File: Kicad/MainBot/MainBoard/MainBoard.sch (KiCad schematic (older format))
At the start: 37 parts, among them J1 Conn_01x02, J10 Conn_01x24, J11 01x24, J12 Conn_01x05, J13 Conn_01x03, J14 Conn_01x03, J15 Conn_01x03, J16 Conn_01x04, J17 Conn_01x04, J18 Conn_01x04, J19 Conn_01x04, J20 Conn_01x03, U1 AZ1117-3.3, U2 TCA9548A, U3 Teensy3.6, U4 DRV8825, U5 DRV8825, U6 DRV8825, U7 DRV8825

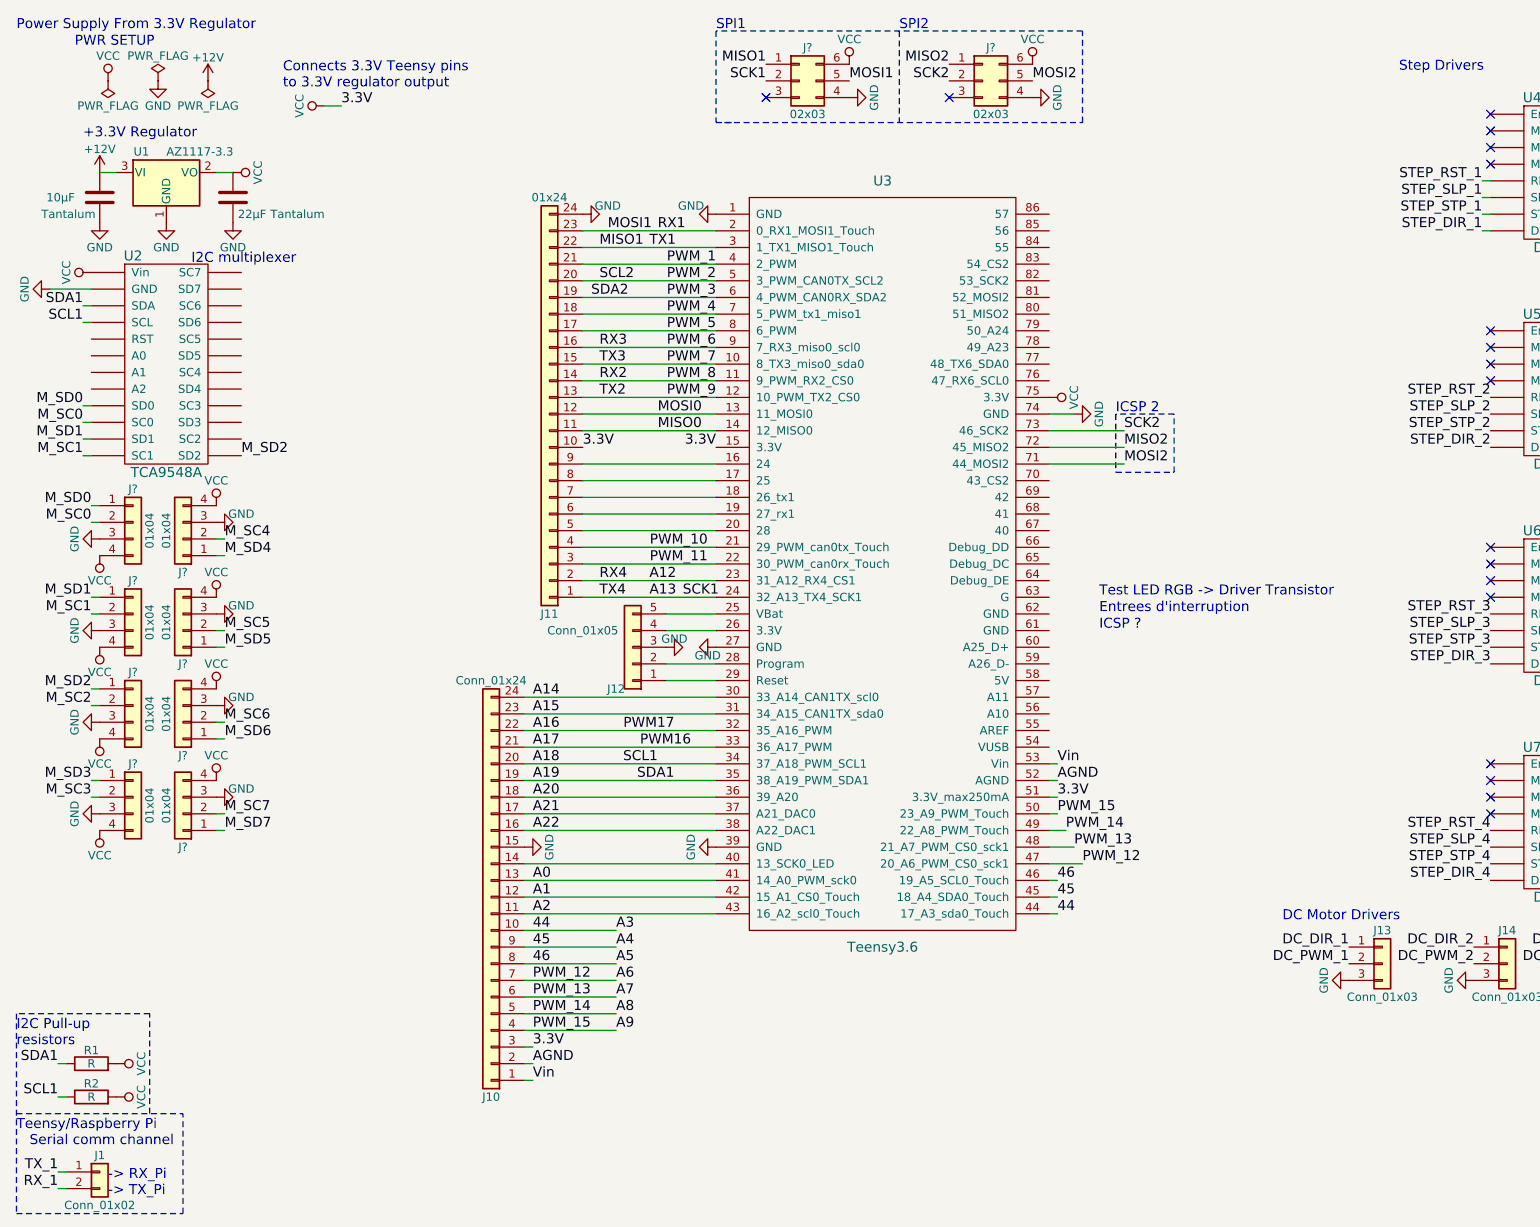
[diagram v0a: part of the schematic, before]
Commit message: Finished Multiplexer output, added pulled up resistors to multiplexer output
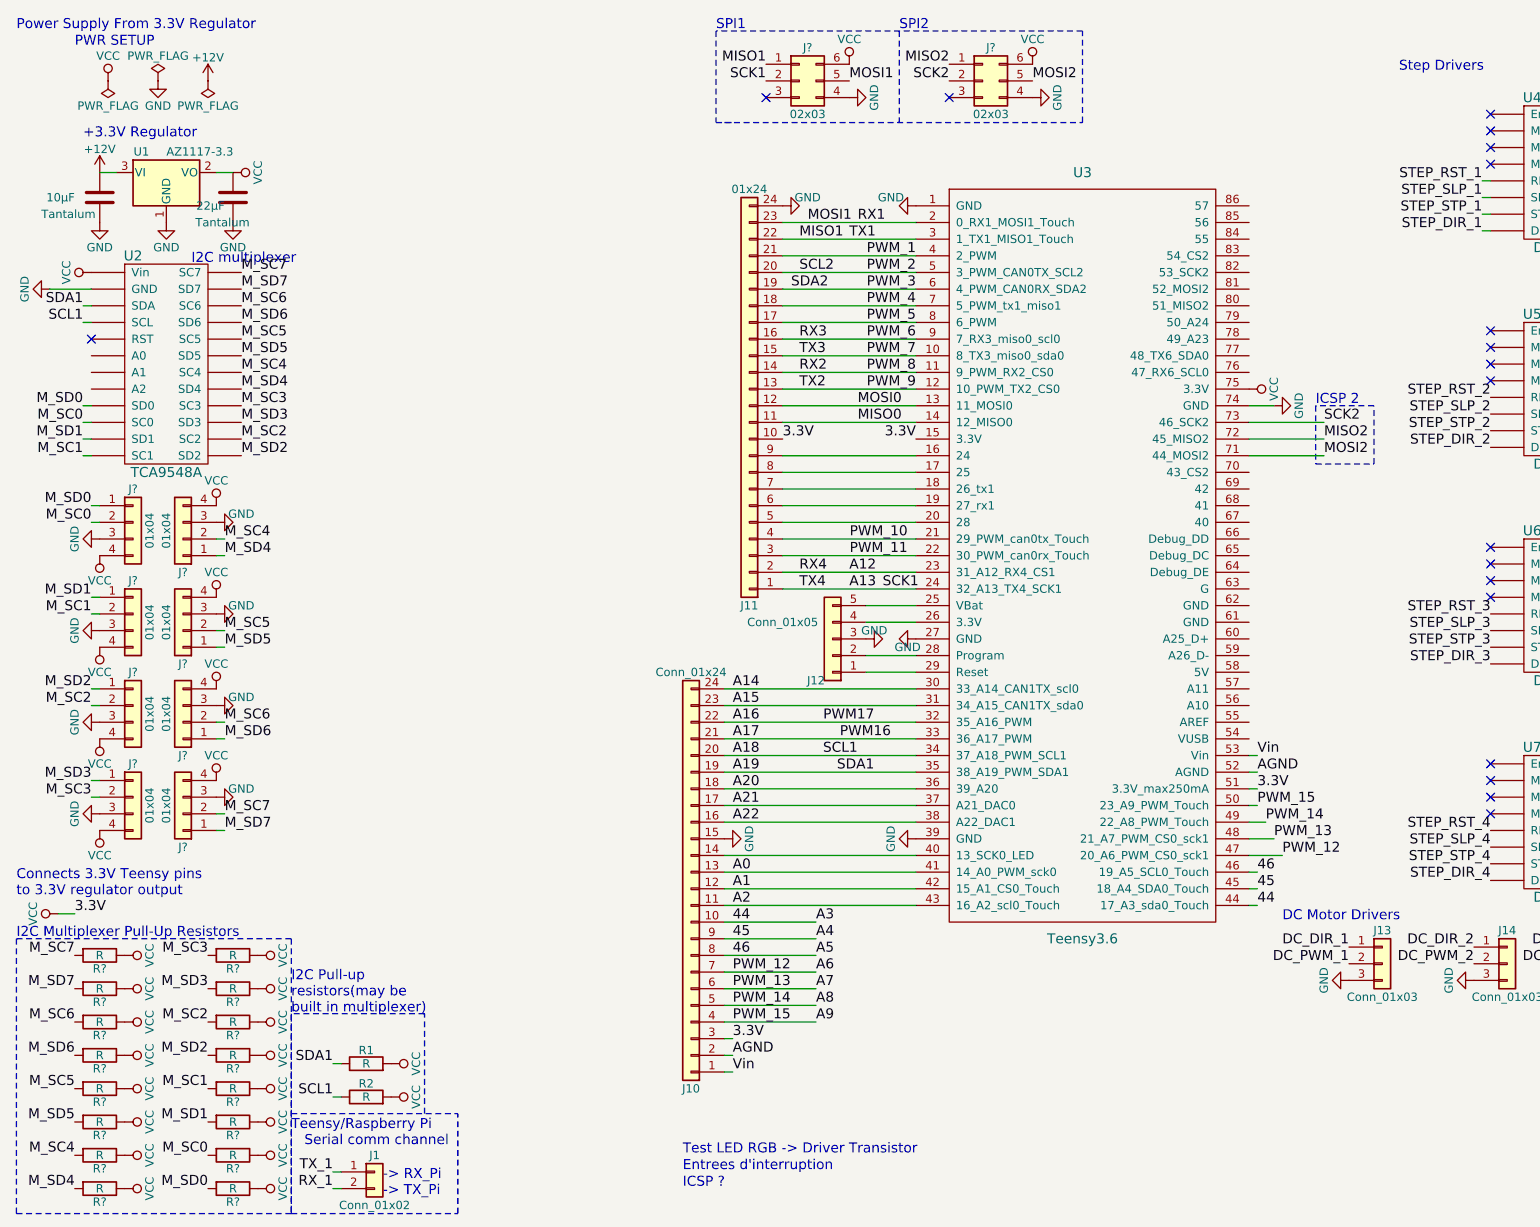
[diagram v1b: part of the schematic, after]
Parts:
- added R? (x16): R, symbol R
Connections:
- net M_SC0: now also R?.2
- net M_SC1: now also R?.2
- net M_SC2: now also U2.~ (Vin), R?.2
- net M_SC3: now also U2.~ (Vin), R?.2
- net M_SC4: now also U2.~ (Vin), R?.2
- net M_SC5: now also U2.~ (Vin), R?.2
- net M_SC6: now also U2.~ (Vin), R?.2
- net M_SC7: now also U2.~ (Vin), R?.2
- net M_SD0: now also R?.2
- net M_SD1: now also R?.2
- net M_SD2: now also R?.2
- net M_SD3: now also U2.~ (Vin), R?.2
- net M_SD4: now also U2.~ (Vin), R?.2
- net M_SD5: now also U2.~ (Vin), R?.2
- net M_SD6: now also U2.~ (Vin), R?.2
- net M_SD7: now also U2.~ (Vin), R?.2
- net VCC: now also R?.1, R?.1, R?.1, R?.1, R?.1, R?.1, R?.1, R?.1, R?.1, R?.1, R?.1, R?.1, R?.1, R?.1, R?.1, R?.1
- no-connect marks 22 -> 23
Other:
- note added: "I2C Multiplexer Pull-Up Resistors\n"
- note added: "I2C Pull-up\nresistors(may be \nbuilt in multiplexer)\n\n"
- note removed: "I2C Pull-up\nresistors\n"
- moved on the sheet: J1, J10, J11, J12, R1, R2, U3

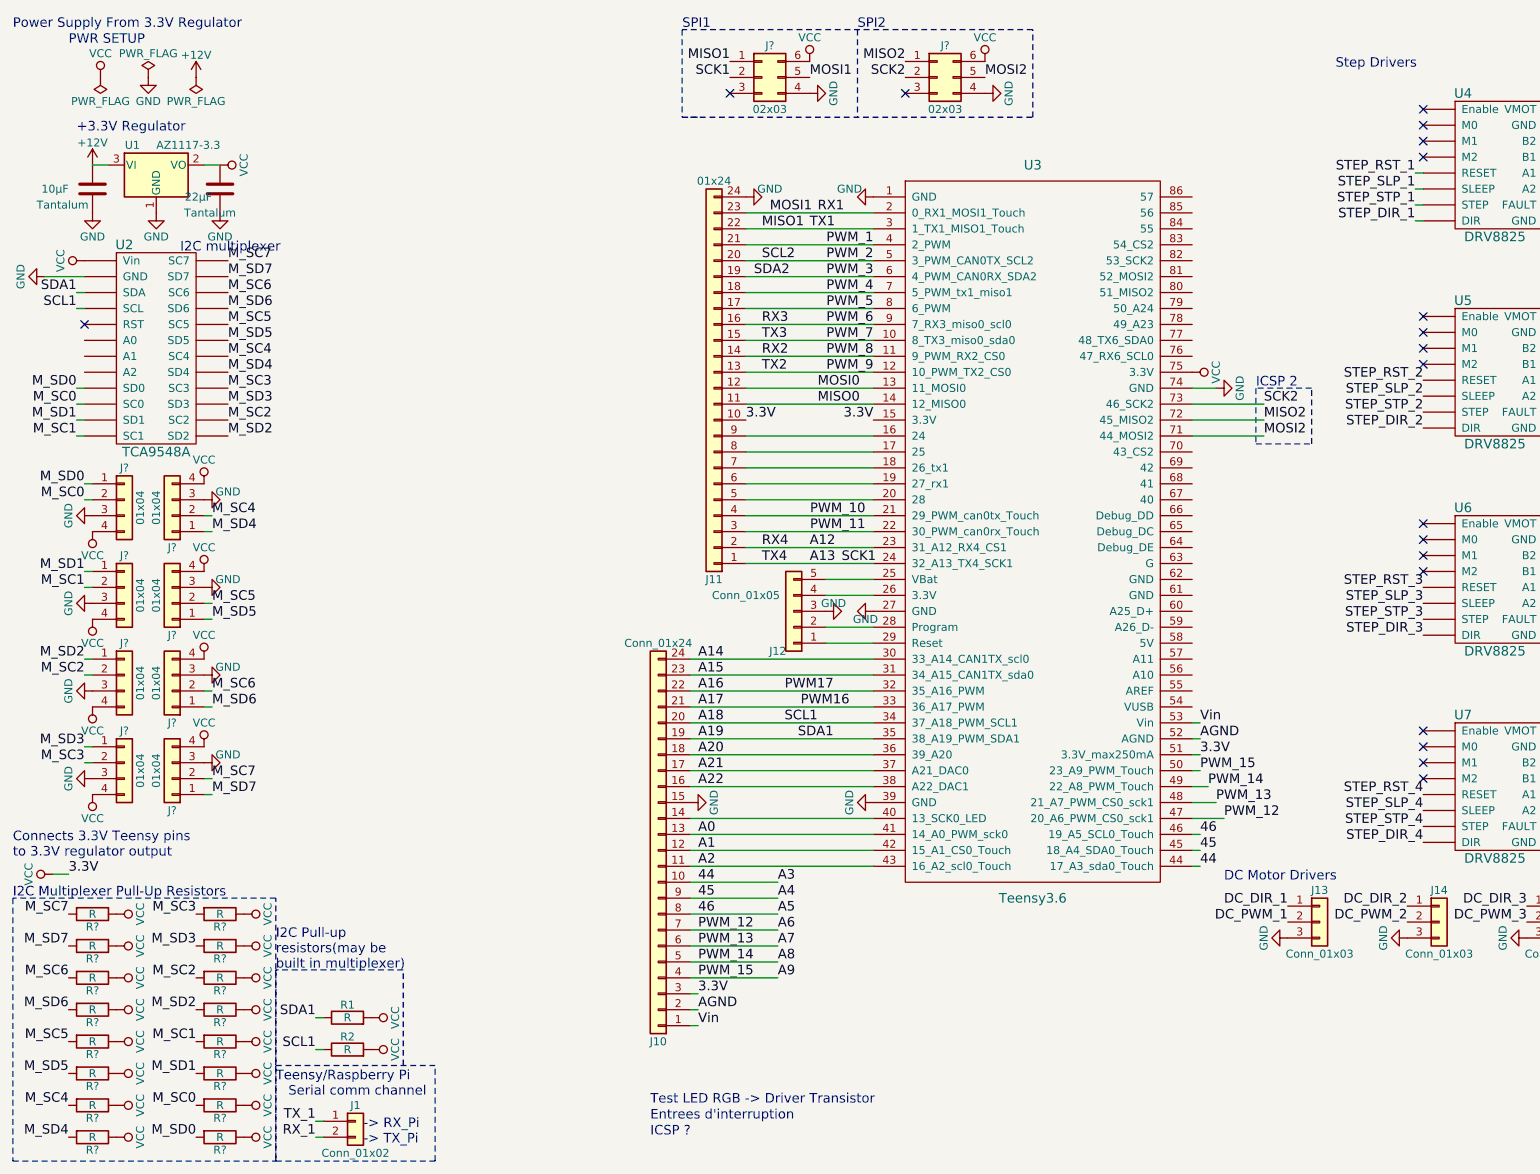
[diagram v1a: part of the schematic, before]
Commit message: Removed NC on DRV8825 Step drivers
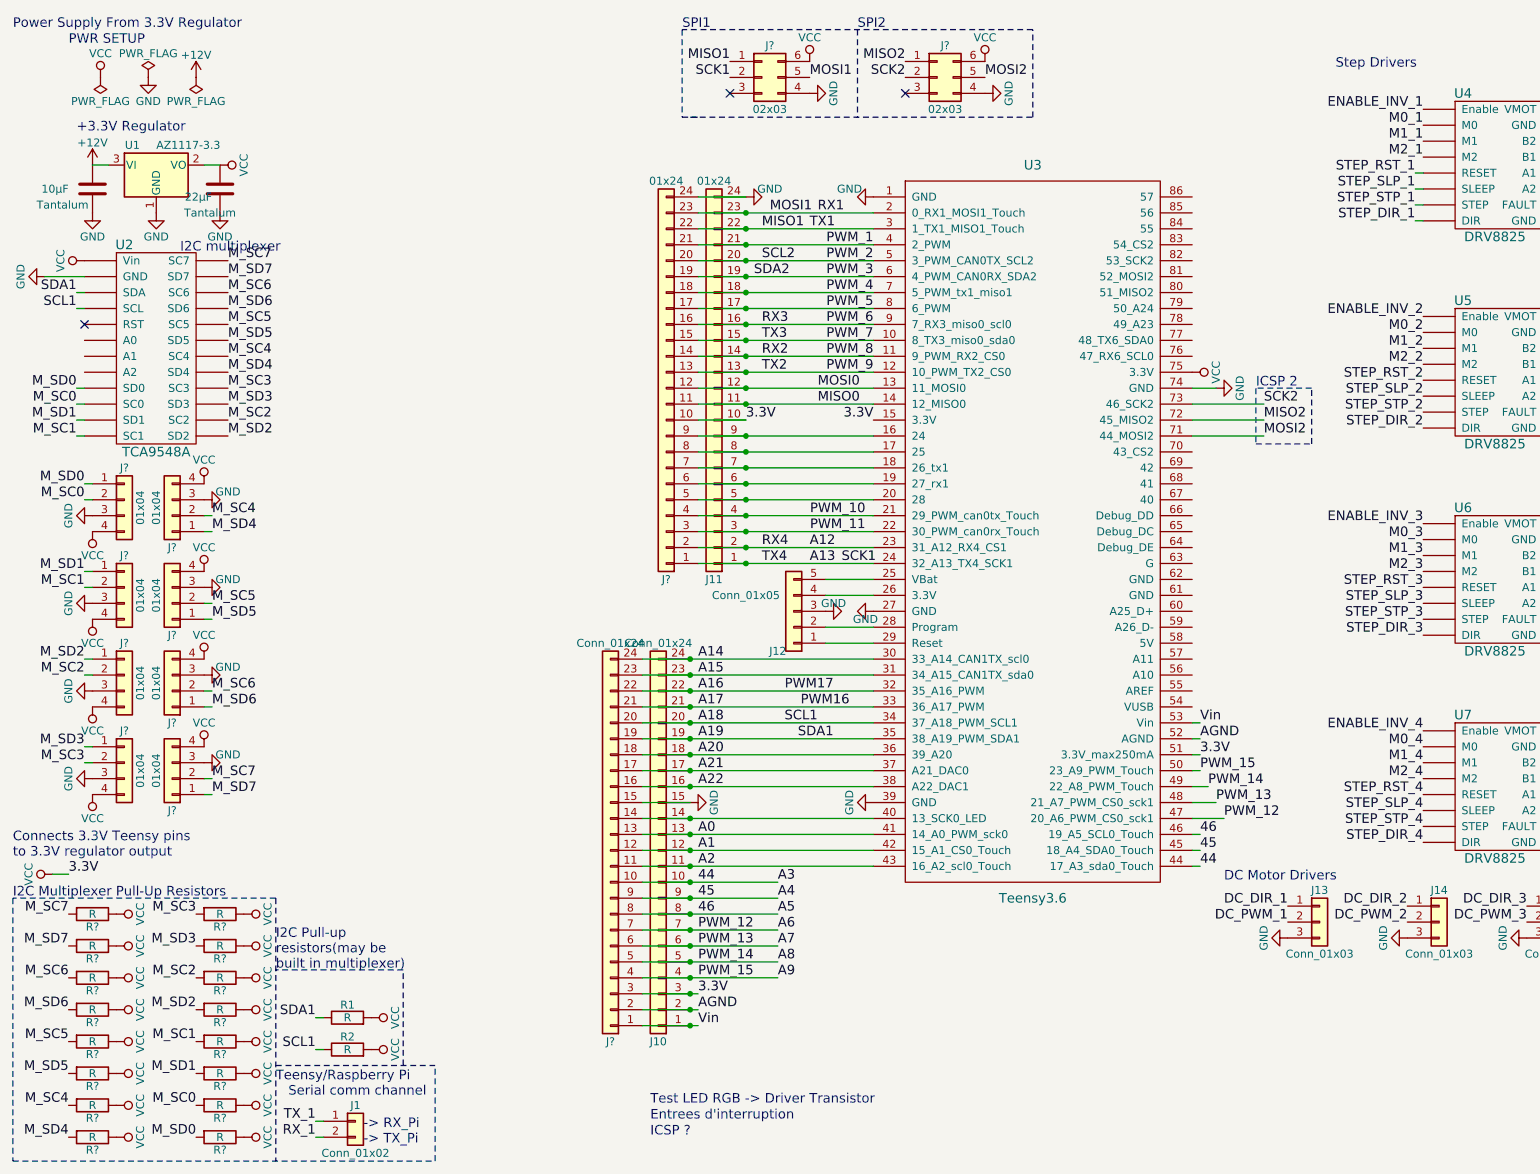
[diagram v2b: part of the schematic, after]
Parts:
- added J?: 01x24, Pin_Headers:Pin_Header_Straight_1x24_Pitch2.54mm, symbol Conn_01x24
- added J?: Conn_01x24, Pin_Headers:Pin_Header_Straight_1x24_Pitch2.54mm, symbol Conn_01x24
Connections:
- net 44: now also J?.10 (Pin_10)
- net 45: now also J?.9 (Pin_9)
- net 46: now also J?.8 (Pin_8)
- net A0: now also J?.13 (Pin_13)
- net A1: now also J?.12 (Pin_12)
- net A12: now also J?.2 (Pin_2)
- net A13: now also J?.1 (Pin_1)
- net A14: now also J?.24 (Pin_24)
- net A15: now also J?.23 (Pin_23)
- net A16: now also J?.22 (Pin_22)
- net A17: now also J?.21 (Pin_21)
- net A18: now also J?.20 (Pin_20)
- net A19: now also J?.19 (Pin_19)
- net A2: now also J?.11 (Pin_11)
- net A20: now also J?.18 (Pin_18)
- net A21: now also J?.17 (Pin_17)
- net A22: now also J?.16 (Pin_16)
- net A6: now also J?.7 (Pin_7)
- net A7: now also J?.6 (Pin_6)
- net A8: now also J?.5 (Pin_5)
- net A9: now also J?.4 (Pin_4)
- net AGND: now also J?.2 (Pin_2)
- net GND: now also J?.15 (Pin_15), J?.24 (Pin_24)
- net MISO0: now also J?.11 (Pin_11)
- net MISO1: now also J?.22 (Pin_22)
- net MOSI0: now also J?.12 (Pin_12)
- net MOSI1: now also J?.23 (Pin_23)
- net PWM_1: now also J?.21 (Pin_21)
- net PWM_10: now also J?.4 (Pin_4)
- net PWM_11: now also J?.3 (Pin_3)
- net PWM_2: now also J?.20 (Pin_20)
- net PWM_3: now also J?.19 (Pin_19)
- net PWM_4: now also J?.18 (Pin_18)
- net PWM_5: now also J?.17 (Pin_17)
- net PWM_6: now also J?.16 (Pin_16)
- net PWM_7: now also J?.15 (Pin_15)
- net PWM_8: now also J?.14 (Pin_14)
- net PWM_9: now also J?.13 (Pin_13)
- net VCC: now also J?.10 (Pin_10), J?.3 (Pin_3)
- net Vin: now also J?.1 (Pin_1)
- net at J11.9 (Pin_9), U3.16 (24): now also J?.9 (Pin_9)
- net at J11.8 (Pin_8), U3.17 (25): now also J?.8 (Pin_8)
- net at J11.7 (Pin_7), U3.18 (26_tx1): now also J?.7 (Pin_7)
- net at J11.6 (Pin_6), U3.19 (27_rx1): now also J?.6 (Pin_6)
- net at J11.5 (Pin_5), U3.20 (28): now also J?.5 (Pin_5)
- net at J10.14 (Pin_14), U3.40 (13_SCK0_LED): now also J?.14 (Pin_14)
- new net ENABLE_INV_1: U4.~ (VMOT)
- new net ENABLE_INV_2: U5.~ (VMOT)
- new net ENABLE_INV_3: U6.~ (VMOT)
- new net ENABLE_INV_4: U7.~ (VMOT)
- new net M0_1: U4.~ (VMOT)
- new net M0_2: U5.~ (VMOT)
- new net M0_3: U6.~ (VMOT)
- new net M0_4: U7.~ (VMOT)
- new net M1_1: U4.~ (VMOT)
- new net M1_2: U5.~ (VMOT)
- new net M1_3: U6.~ (VMOT)
- new net M1_4: U7.~ (VMOT)
- new net M2_1: U4.~ (VMOT)
- new net M2_2: U5.~ (VMOT)
- new net M2_3: U6.~ (VMOT)
- new net M2_4: U7.~ (VMOT)
- no-connect marks 23 -> 7
